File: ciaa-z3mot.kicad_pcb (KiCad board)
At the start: 2 copper layers, 18.8 x 67.7 mm, 76 parts, among them J1 Conn_01x20, J2 Conn_01x20, J3 Conn_01x02, J4 SWD, J5 USB_OTG, J6 Conn_Coaxial, J7 Conn_01x05, J8 Conn_Coaxial, SW1 reset, SW2 reset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

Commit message: mejoras 1
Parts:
- removed J3: Conn_01x02, Connector_PinHeader_2.54mm:PinHeader_1x02_P2.54mm_Vertical
- added D4: ON, footprints:LED_0805, F.Cu at (128.3, 72.5)
- added R12: 1K, Resistor_SMD:R_0402_1005Metric, F.Cu at (128.1, 74.8)
- moved C13 39.2 mm to (131.7, 116.8)
- moved R1 36.6 mm to (122.3, 87.3), turned to 90 degrees
- moved L1 15.2 mm to (131.7, 89.1), turned to 180 degrees
- moved C17 12.9 mm to (133.0, 96.2), turned to 270 degrees
- moved C42 12.1 mm to (122.5, 84.8)
- moved C18 5.99 mm to (133.0, 97.9)
- moved C8 3.40 mm to (128.2, 89.0)
- moved C7 1.99 mm to (122.2, 92.2), turned to 180 degrees
- moved C9 1.69 mm to (129.9, 89.8), turned to 90 degrees
- moved C32 0.96 mm to (130.1, 103.8)
- moved C27 0.91 mm to (128.5, 103.9)
- moved C14 0.88 mm to (131.6, 90.8)
- moved C11 0.87 mm to (132.6, 90.8)
- moved Y2 0.86 mm to (129.3, 102.6)
- moved U2 0.59 mm to (125.1, 88.4)
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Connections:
- net /B_USB+ renamed Net-(J5-Pad3)
- net /B_USB- renamed Net-(J5-Pad2)
- net /PA10 renamed /GPIO01
- J1 pad 16: /PA9 -> /GPIO0 (x2)
- J1 pad 17: /PA8 -> +3V3 (x2)
- J1 pad 19: GND -> /On (x2)
- J1 pad 20: GND -> /Bat (x2)
- J2 pad 13: /PA2 -> /ENA (x2)
- J2 pad 14: /PC0 -> /GPIO03 (x2)
- J2 pad 15: /PC1 -> GND (x2)
- R4 pad 2: /PA8 -> +3V3
- U1 pad 15: /PA2 -> /ENA
- U1 pad 16: /PC0 -> /GPIO03
- U1 pad 25: /PA9 -> /GPIO00
- U2 pad 1: (no net) -> /GPIO00
- U2 pad 3: (no net) -> /GPIO03
- U2 pad 4: (no net) -> /ENA
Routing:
- net /PC0: track 32.2 -> 0.00 mm, vias 2 -> 0
- net /nRESET: track 6.31 -> 36.7 mm, vias 4 -> 2
- net VMCU: track 5.38 -> 30.1 mm, vias 2 -> 6
- net /GPIO03: track 0.00 -> 23.1 mm, vias 0 -> 2
- net /PF0/SWCLK: track 4.47 -> 27.2 mm
- net /ENA: track 0.00 -> 19.3 mm, vias 0 -> 2
- net /PF1/SWDIO: track 5.85 -> 25.0 mm
- net /USB+: track 2.51 -> 19.1 mm
- net /GPIO00: track 0.00 -> 16.1 mm, vias 0 -> 2
- net /On: track 5.73 -> 20.5 mm
- net +3V3: track 28.4 -> 14.1 mm, vias 5 -> 4
- net Net-(J5-Pad2): track 0.00 -> 13.5 mm, vias 0 -> 1
- net Net-(J5-Pad3): track 0.00 -> 13.3 mm, vias 0 -> 1
- net GND: track 52.9 -> 40.8 mm, vias 11 -> 10
- net Net-(J5-Pad6): track 0.00 -> 12.1 mm, vias 1 -> 0
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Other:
- outline, holes or cut-outs redrawn

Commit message: sin verificar ruteo gnd
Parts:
- removed D4: ON, footprints:LED_0805
- removed J5: USB_OTG, footprints:USB_Micro-B_Molex_47346-0001
- added ON: Conn_01x02, Connector_PinHeader_1.27mm:PinHeader_1x02_P1.27mm_Vertical, F.Cu at (133.0, 71.8)
- added R13: 0R, Resistor_SMD:R_0201_0603Metric, F.Cu at (130.4, 106.3)
- added USB: Conn_01x04, Connector_PinHeader_1.27mm:PinHeader_1x04_P1.27mm_Vertical, F.Cu at (129.0, 69.6)
- R12: value 1K -> 0R; footprint Resistor_SMD:R_0402_1005Metric -> Resistor_SMD:R_0201_0603Metric
- moved R12 31.7 mm to (131.0, 106.3), turned to 90 degrees
- moved D3 2.78 mm to (128.8, 72.2)
- moved C22 2.37 mm to (129.5, 74.8), turned to 0 degrees
- moved C33 2.01 mm to (131.2, 72.5), turned to 90 degrees
- moved C39 1.20 mm to (132.1, 101.0)
- moved Y3 1.16 mm to (131.7, 102.6)
- moved C41 0.81 mm to (131.9, 104.3)
- moved U5 0.56 mm to (127.1, 65.0)
- moved C32 0.47 mm to (129.9, 104.3)
- moved C27 0.45 mm to (128.3, 104.3)
- moved C42 0.14 mm to (122.3, 84.8)
- moved U3 0.12 mm to (125.4, 72.3)
- renumbered J7 to JTAG
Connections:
- BT1 pad 3: (no net) -> GND
- J1 pad 17: +3V3 -> /PA8 (x2)
- J1 pad 19: /On -> GND (x2)
- J1 pad 20: /Bat -> GND (x2)
- J2 pad 16: /PC2 -> GND (x2)
- J2 pad 18: /PC4 -> GND (x2)
- J2 pad 19: LFXTAL_P -> /PB7 (x2)
- J2 pad 20: LFXTAL_N -> /PB8 (x2)
- R12 pad 1: Net-(D4-Pad2) -> /PB8
- R12 pad 2: +3V3 -> LFXTAL_N
- R3 pad 2: LFXTAL_N -> /PB8
- R4 pad 2: +3V3 -> /PA8
- SW1 pad 2: LFXTAL_N -> /PB8
- U1 pad : (no net) -> GND
- U1 pad 25: /GPIO00 -> /GPIO0
- U2 pad 1: /GPIO00 -> /GPIO0
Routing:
- net +3V3: track 14.1 -> 93.8 mm, vias 4 -> 6
- net GND: track 40.8 -> 118.2 mm, vias 10 -> 19
- net /GPIO0: track 0.01 -> 26.8 mm, vias 0 -> 2
- net /nRESET: track 36.7 -> 62.1 mm, vias 2 -> 1
- net /PB8: track 0.00 -> 24.0 mm, vias 0 -> 1
- net /+5V: track 0.00 -> 18.6 mm
- net /PB7: track 0.00 -> 18.0 mm, vias 0 -> 1
- net /vusb: track 21.1 -> 37.9 mm
- net /GPIO00: track 16.1 -> 0.00 mm, vias 2 -> 0
- net Net-(J5-Pad6): track 12.1 -> 0.00 mm
- net /GPIO01: track 1.46 -> 10.7 mm
- net /Bat: track 1.82 -> 10.8 mm
- net /PC9: track 4.76 -> 13.6 mm
- net /PC10: track 7.08 -> 15.8 mm
- net /PB11: track 3.00 -> 10.4 mm
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- added copper zone on F.Cu, net GND
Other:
- outline, holes or cut-outs redrawn

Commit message: render completo y cambio smd pack
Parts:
- C33: footprint Capacitor_SMD:C_0603_1608Metric -> Capacitor_SMD:C_0805_2012Metric
- C42: footprint footprints:C_0603 -> Capacitor_SMD:C_1206_3216Metric
- moved C42 0.98 mm to (122.4, 83.9)
- moved U2 0.57 mm to (125.3, 89.0), turned to 270 degrees
- moved R1 0.49 mm to (121.9, 87.3)
- moved Y3 0.44 mm to (132.0, 102.3)
- moved L1 0.42 mm to (132.1, 89.1)
- moved C39 0.41 mm to (132.4, 100.6)
- moved J4 0.33 mm to (122.5, 80.8)
- moved L10 0.26 mm to (125.7, 82.0)
- moved D1 0.23 mm to (126.2, 119.5)
- moved D2 0.23 mm to (127.9, 119.5)
- moved SW1 0.23 mm to (123.1, 119.8)
- moved SW2 0.23 mm to (131.0, 119.8)
- moved U4 0.20 mm to (125.3, 85.2), turned to 90 degrees
- moved C14 0.20 mm to (131.6, 91.0)
- moved C11 0.20 mm to (132.7, 91.0)
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- renumbered ON to J3, JTAG to J7
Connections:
- BT1 pad 3: GND -> (no net)
- U1 pad : GND -> (no net)
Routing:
- net GND: track 118.2 -> 238.1 mm, vias 19 -> 20
- net /PA8: track 0.00 -> 15.2 mm, vias 0 -> 3
- net /ENA: track 19.6 -> 16.0 mm
- net /GPIO0: track 26.8 -> 28.6 mm
- net +3V3: track 93.8 -> 95.6 mm, vias 6 -> 5
- net /nRESET: track 62.1 -> 60.4 mm
- net VMCU: track 34.1 -> 35.9 mm, vias 6 -> 7
- net /USB-: track 21.6 -> 20.0 mm
- net /Ldo: track 5.45 -> 4.24 mm
- net /vusb: track 37.9 -> 36.9 mm
- net /PF1/SWDIO: track 25.0 -> 25.9 mm
- net /PF0/SWCLK: track 27.2 -> 28.0 mm
- net /GPIO03: track 23.1 -> 22.5 mm
- net HFXTAL_P: track 8.44 -> 7.78 mm
- net /PF2: track 19.0 -> 19.7 mm
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
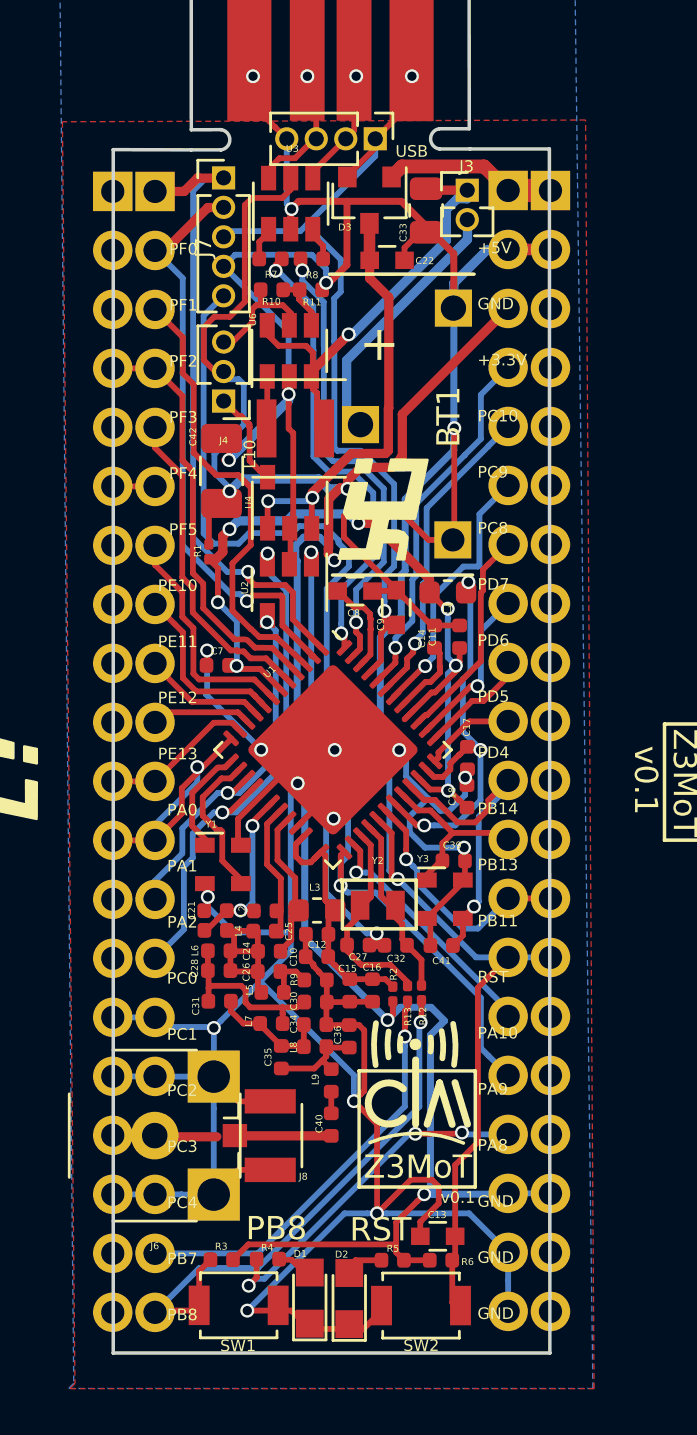
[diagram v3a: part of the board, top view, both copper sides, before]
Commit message: agrego porta baterias
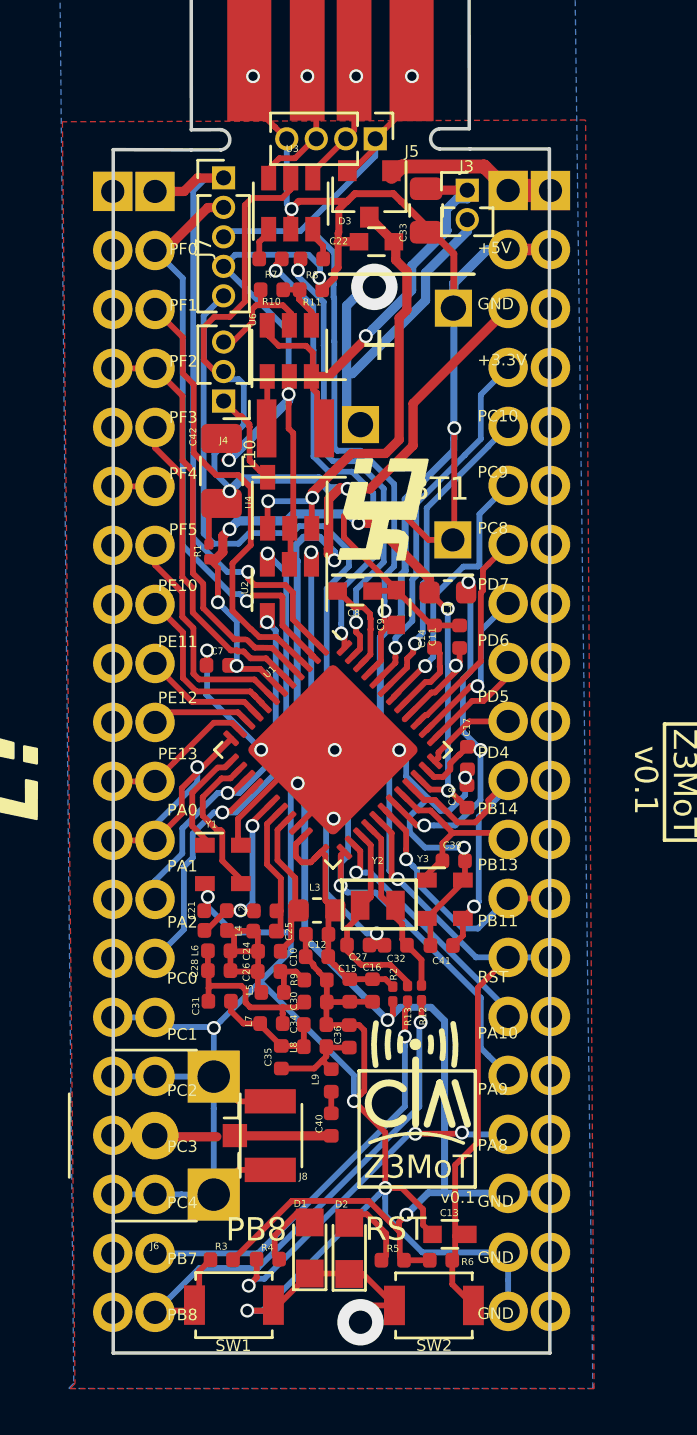
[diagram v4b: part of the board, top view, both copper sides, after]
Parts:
- moved D1 2.16 mm to (126.2, 117.3)
- moved D2 2.16 mm to (127.9, 117.3)
- moved C22 0.92 mm to (129.1, 74.0), turned to 180 degrees
- moved SW2 0.56 mm to (131.5, 119.8)
- moved C13 0.53 mm to (132.2, 116.7)
- moved D3 0.27 mm to (128.8, 71.9)
- moved SW1 0.20 mm to (122.9, 119.8)
- renumbered USB to J5
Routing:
- net /Bat: track 11.3 -> 15.4 mm, vias 0 -> 1
- net Net-(D1-Pad2): track 1.61 -> 3.21 mm
- net Net-(D2-Pad2): track 2.01 -> 3.47 mm
- net GND: track 238.1 -> 239.3 mm, vias 20 -> 21
- net /+5V: track 18.9 -> 19.8 mm
- net /nRESET: track 60.4 -> 60.9 mm
